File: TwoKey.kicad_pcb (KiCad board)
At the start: 2 copper layers, 34 parts, among them J1 USB_C_Receptacle_USB2.0, SW1 SW_SPST, SW2 SW_SPST, SW3 BOOTSEL, SW4 RESET, U1 AMS1117-3.3, U2 W25Q128JVS, U3 RP2040TR7, X1 OSC

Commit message: Started work on condencing items
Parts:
- J1: moved to B.Cu
- moved C1 50.5 mm to (33.3, 43.0)
- moved C2 50.5 mm to (41.0, 37.7)
- moved U1 50.5 mm to (35.7, 38.5)
- moved C10 50.1 mm to (70.7, 58.4)
- moved C11 50.1 mm to (64.8, 63.5)
- moved C12 50.1 mm to (58.3, 64.8)
- moved C13 50.1 mm to (58.5, 58.4)
- moved C14 50.1 mm to (58.5, 54.8)
- moved C16 50.1 mm to (69.8, 51.3)
- moved C6 50.1 mm to (66.8, 51.3)
- moved C8 50.1 mm to (68.3, 51.3)
- moved C9 50.1 mm to (70.7, 54.8)
- moved R7 50.1 mm to (63.3, 65.4)
- moved U2 50.1 mm to (56.8, 49.8)
- moved U3 50.1 mm to (64.6, 57.4)
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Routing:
- net +5V: track 2.21 -> 9.57 mm
- net /USB_DN: track 0.00 -> 2.99 mm, vias 0 -> 1
- net /USB_DP: track 0.00 -> 2.91 mm, vias 0 -> 1
- net GND: track 0.00 -> 2.31 mm, vias 0 -> 2
- net Net-(R6-Pad1): track 4.50 -> 5.70 mm
- net Net-(R5-Pad1): track 4.50 -> 5.70 mm

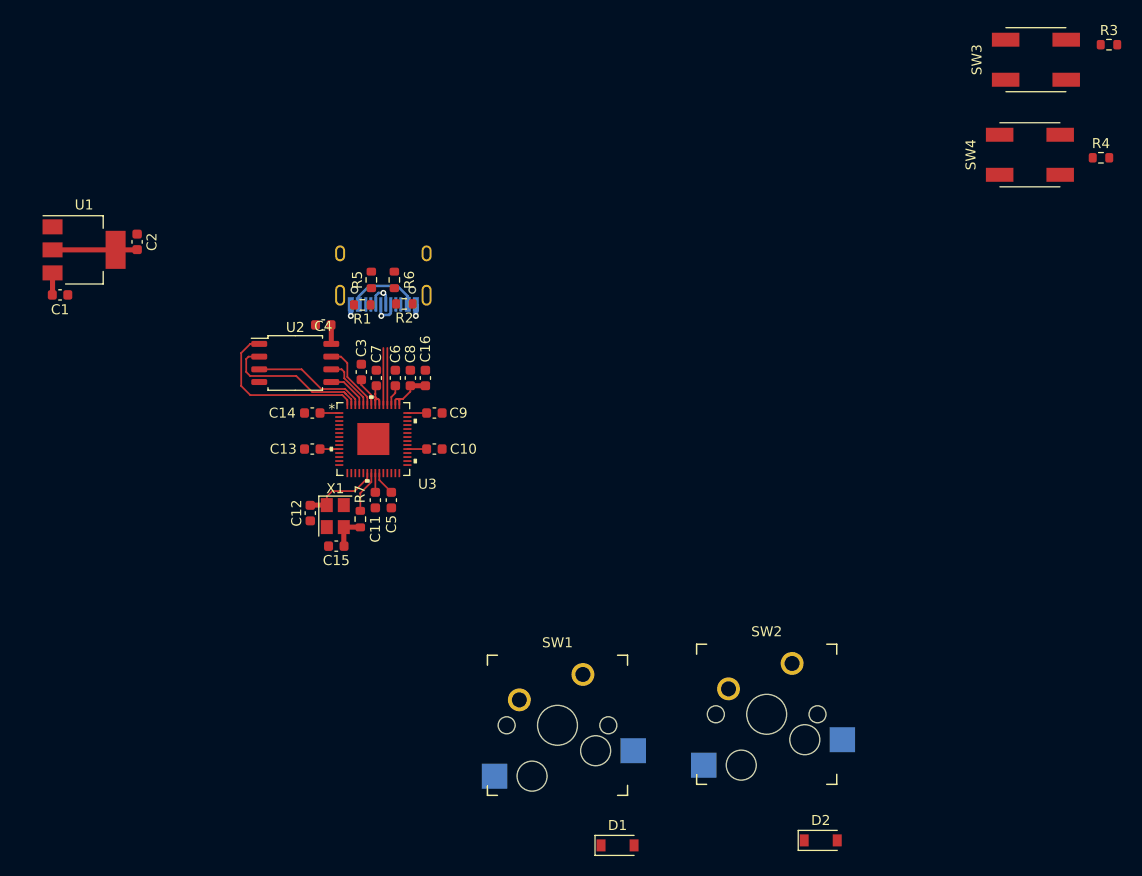
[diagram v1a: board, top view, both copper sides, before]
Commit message: Reworked some placement and added submodule
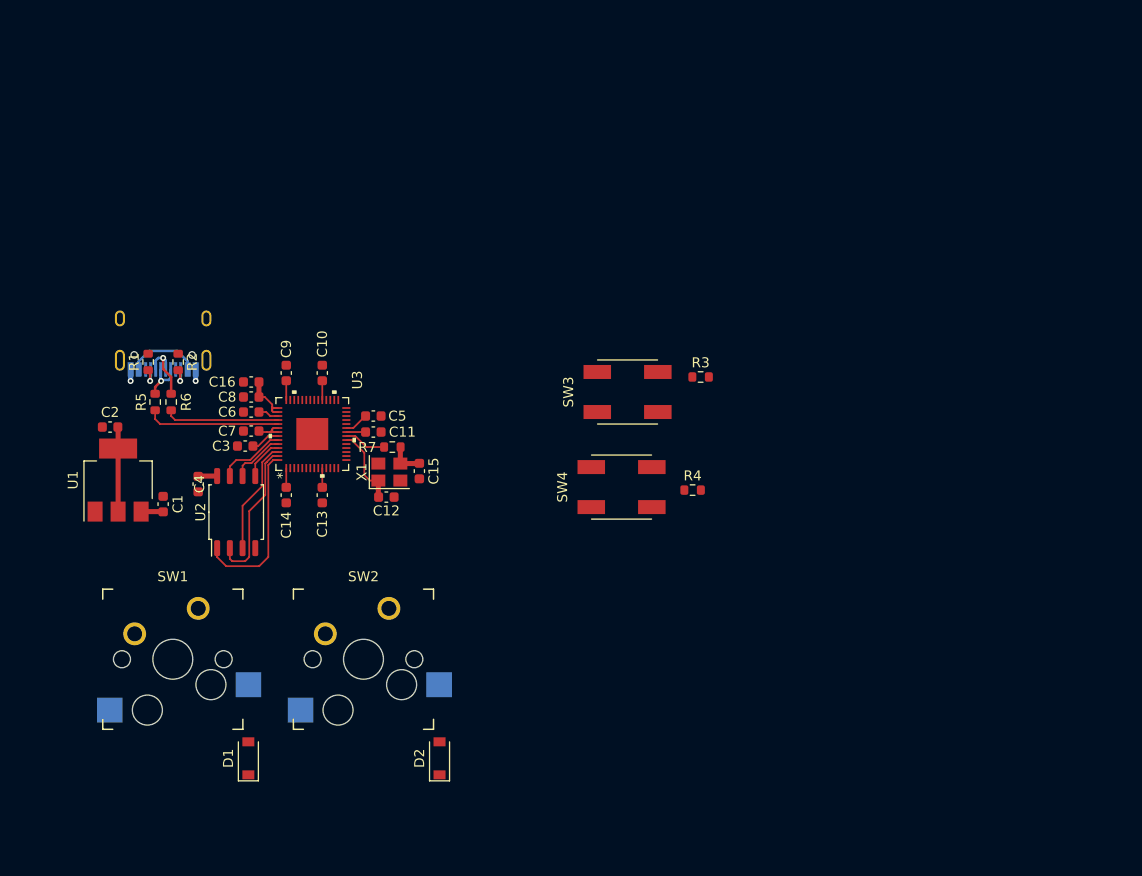
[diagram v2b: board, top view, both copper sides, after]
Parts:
- moved R4 52.6 mm to (96.5, 62.5)
- moved SW3 52.6 mm to (90.0, 52.7)
- moved R3 52.6 mm to (97.3, 51.2)
- moved SW4 52.6 mm to (89.4, 62.2)
- moved SW2 40.7 mm to (63.6, 79.4)
- moved SW1 39.0 mm to (44.6, 79.4)
- moved D2 39.0 mm to (71.2, 89.3), turned to 90 degrees
- moved D1 37.9 mm to (52.1, 89.3), turned to 90 degrees
- moved R6 25.4 mm to (44.4, 53.7), turned to 90 degrees
- moved R5 24.8 mm to (42.8, 53.7), turned to 90 degrees
- moved R2 23.3 mm to (45.1, 49.7), turned to 90 degrees
- moved C1 23.3 mm to (43.6, 63.9), turned to 90 degrees
- moved U1 23.2 mm to (39.1, 61.5), turned to 90 degrees
- moved J1 22.9 mm to (43.6, 46.4)
- moved R1 22.1 mm to (42.1, 49.7), turned to 90 degrees
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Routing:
- net Net-(R5-Pad1): track 5.70 -> 13.4 mm
- net Net-(R6-Pad1): track 5.70 -> 11.4 mm
- net /USB_DN: track 2.99 -> 6.90 mm
- net Net-(J1-PadB5): track 0.00 -> 2.33 mm, vias 0 -> 1
- net Net-(J1-PadA5): track 0.00 -> 2.33 mm, vias 0 -> 1
- net /USB_DP: track 2.91 -> 4.43 mm

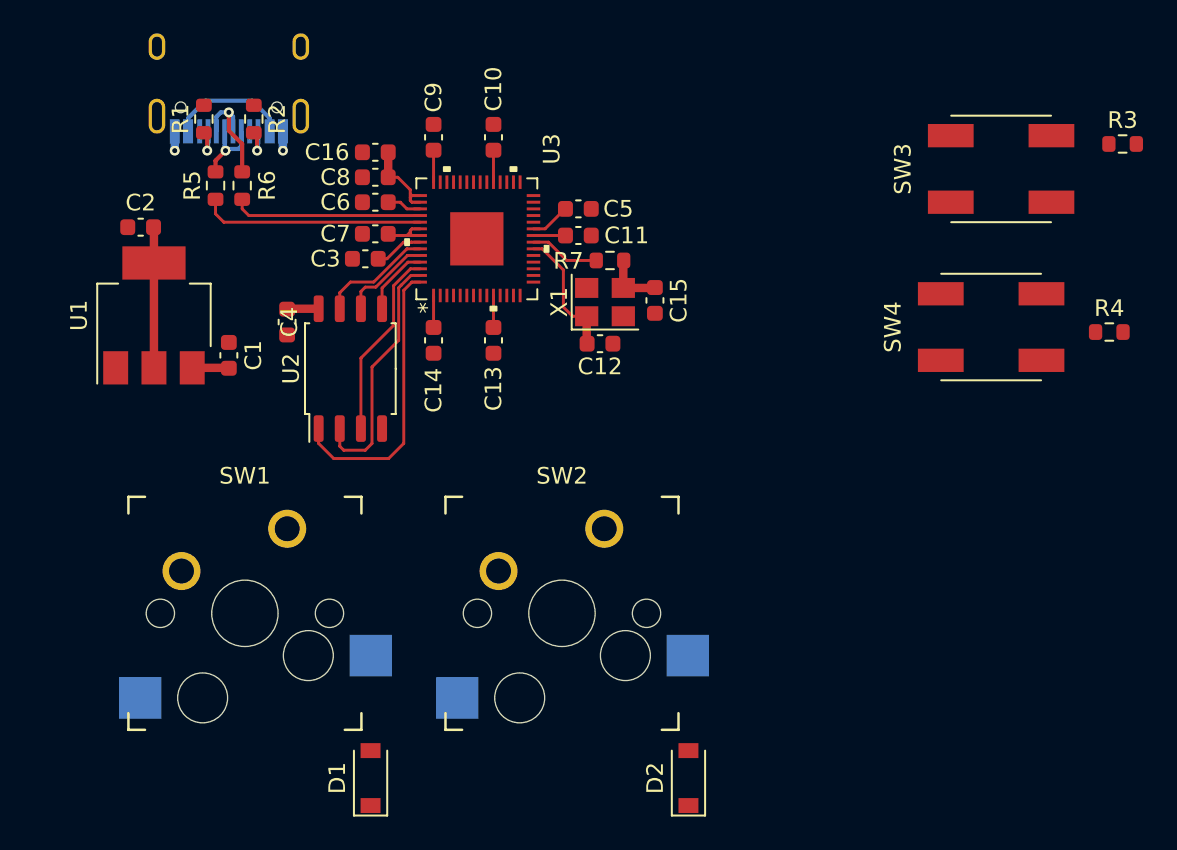
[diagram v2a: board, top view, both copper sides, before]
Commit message: Condenced items into initial pcb
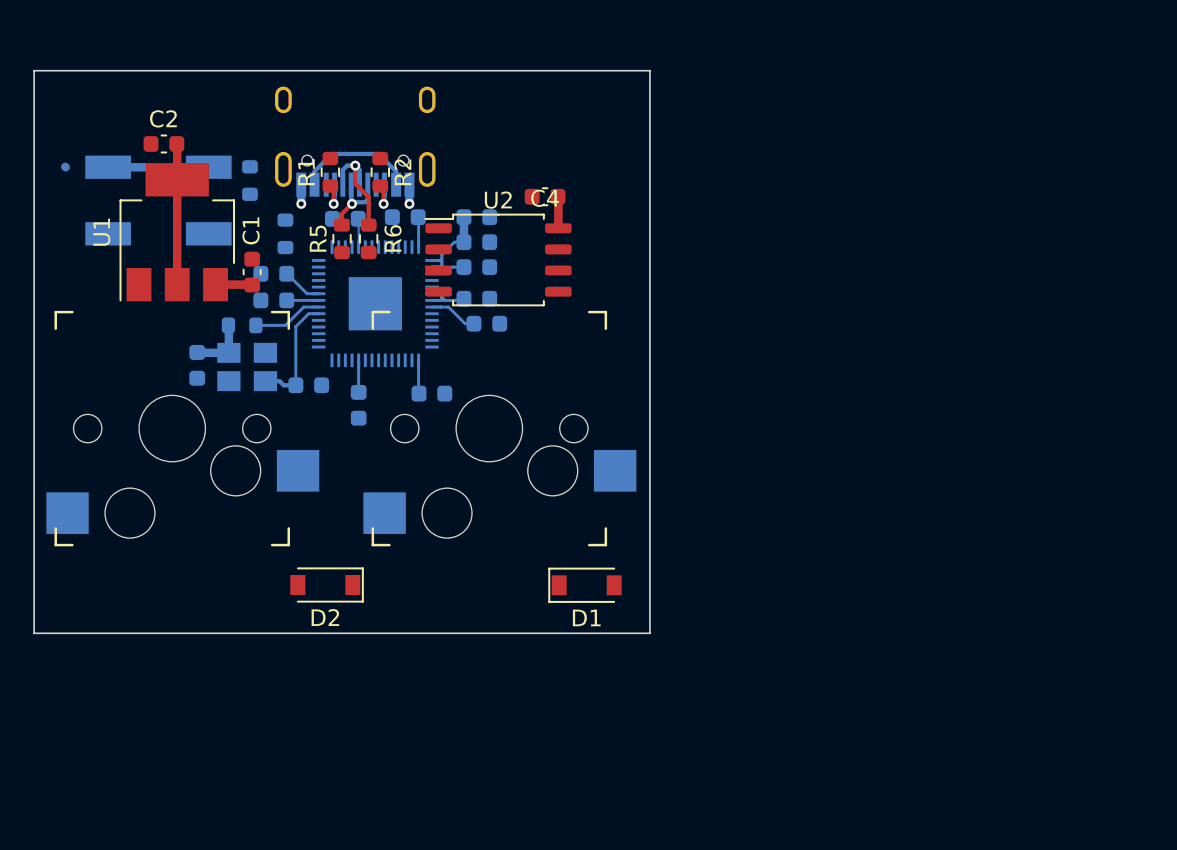
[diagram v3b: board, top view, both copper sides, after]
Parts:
- removed SW4: RESET, TwoKey:DTSL-61N-V
- C10, C11, C12, C13, C14, C15, C16, C3, C5, C6, C7, C8, C9, R3, R4, R7, SW3, U3, X1: moved to B.Cu
- SW1, SW2: footprint keyswitches:Kailh_socket_MX_optional -> keyswitches:Kailh_socket_MX
- moved R3 52.5 mm to (44.9, 53.4), turned to 90 degrees
- moved SW3 50.7 mm to (39.4, 54.6), turned to 180 degrees
- moved R4 49.9 mm to (47.0, 56.6), turned to -90 degrees
- moved C15 27.8 mm to (41.7, 64.5)
- moved SW2 25.9 mm to (40.2, 68.3), turned to 180 degrees
- moved D2 24.7 mm to (49.4, 77.7), turned to 180 degrees
- moved R7 22.4 mm to (44.4, 62.1), turned to 0 degrees
- moved X1 21.9 mm to (44.7, 64.6), turned to 180 degrees
- moved C11 18.7 mm to (46.3, 60.6), turned to 180 degrees
- moved C5 18.7 mm to (46.3, 59.0), turned to 180 degrees
- moved SW1 18.4 mm to (59.2, 68.3), turned to 180 degrees
- moved C12 17.7 mm to (48.4, 65.7)
- moved D1 17.4 mm to (65.1, 77.7), turned to 0 degrees
- moved C4 17.2 mm to (62.6, 54.4), turned to 180 degrees
- moved U2 11.0 mm to (59.8, 58.2), turned to 0 degrees
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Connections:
- SW1 pad 1: /COL1 -> Net-(D1-Pad2)
- SW1 pad 2: Net-(D1-Pad2) -> /COL1
- SW2 pad 1: /COL2 -> Net-(D2-Pad2)
- SW2 pad 2: Net-(D2-Pad2) -> /COL2
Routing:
- net /QSPI_SS: track 17.2 -> 0.00 mm
- net /QSPI_SD1: track 15.0 -> 0.00 mm
- net Net-(R5-Pad1): track 13.4 -> 0.00 mm
- net Net-(R6-Pad1): track 11.4 -> 0.00 mm
- net /QSPI_SD2: track 11.4 -> 0.00 mm
- net /QSPI_SD3: track 6.89 -> 0.00 mm
- net Net-(R3-Pad2): track 0.00 -> 6.09 mm
- net /QSPI_SCLK: track 5.49 -> 0.00 mm
- net /QSPI_SD0: track 4.18 -> 0.00 mm
- net /XIN: track 7.84 -> 7.15 mm
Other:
- board outline added: 37 x 33.8 mm

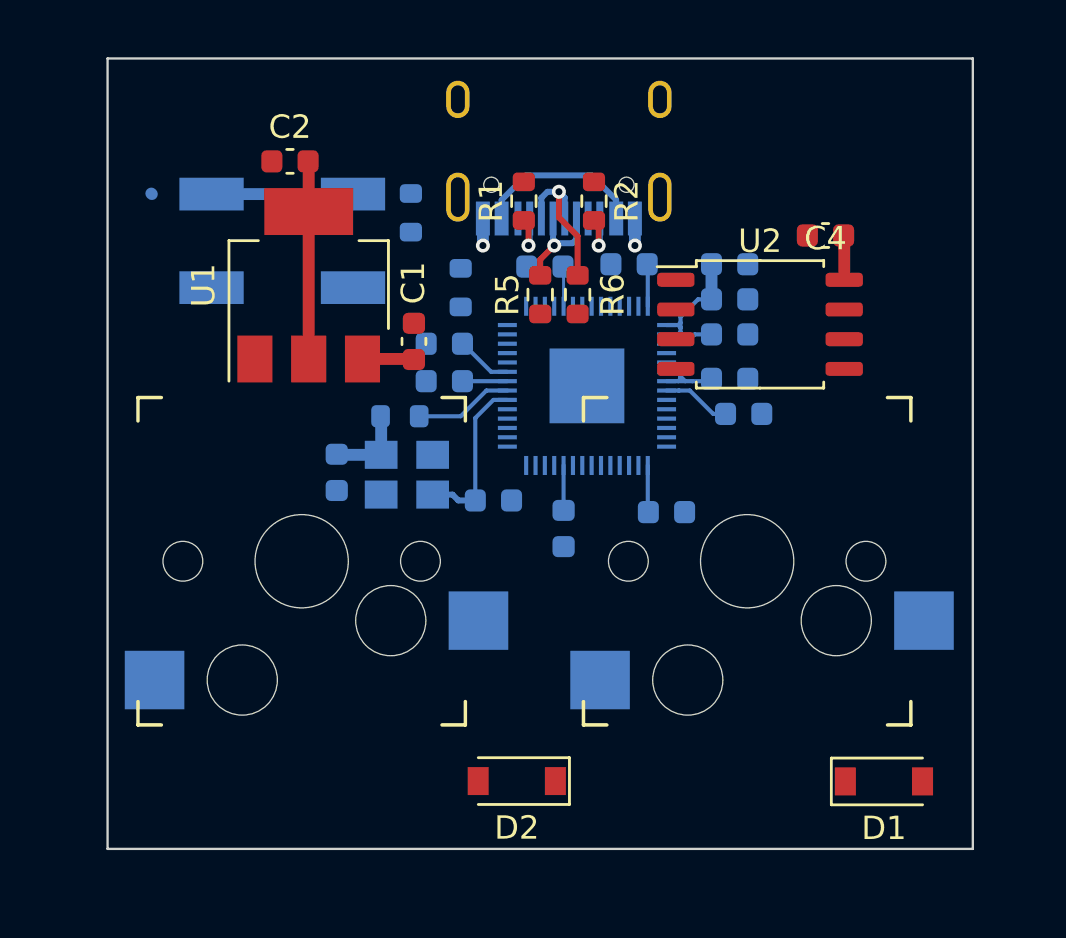
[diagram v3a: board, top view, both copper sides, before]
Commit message: Readjusted more componenets (DRC not passing)
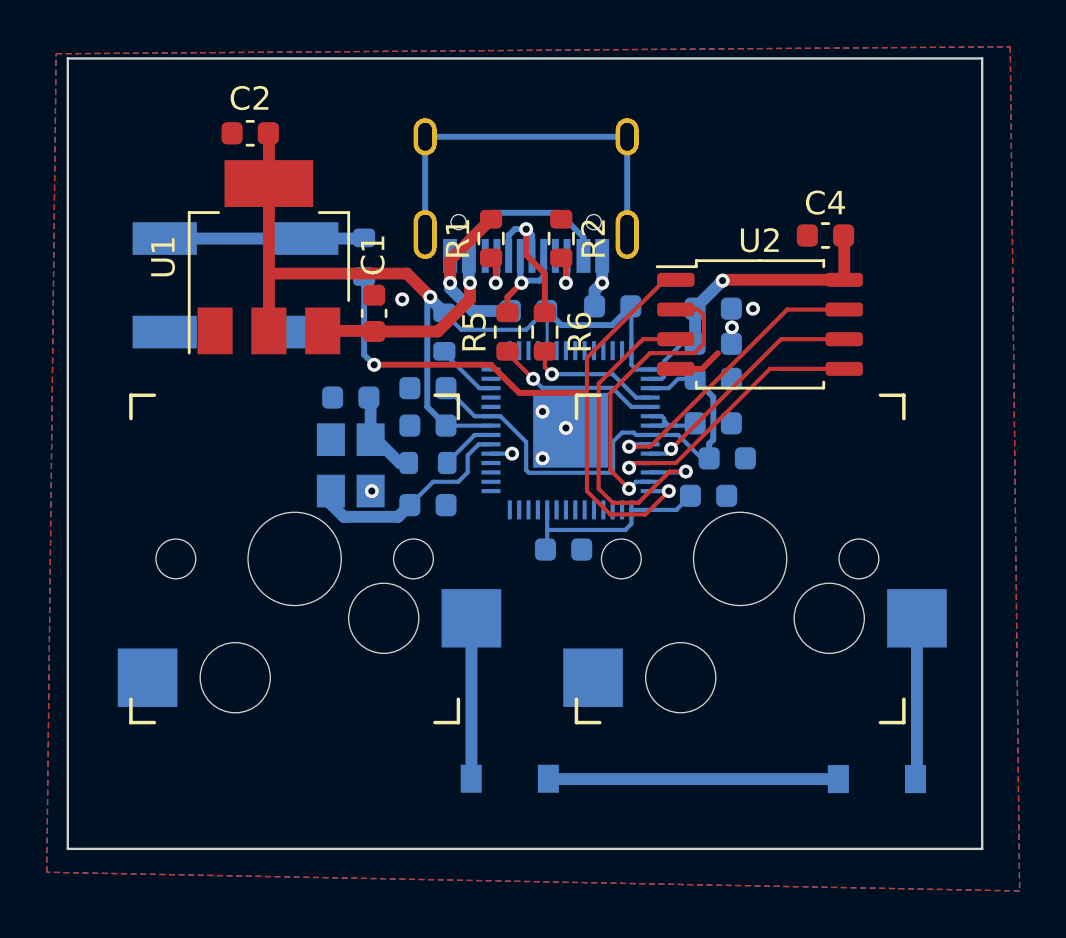
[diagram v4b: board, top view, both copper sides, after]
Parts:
- D1, D2: moved to B.Cu
- moved C15 3.26 mm to (42.3, 61.3), turned to 180 degrees
- moved C12 2.81 mm to (45.6, 65.9)
- moved R3 2.76 mm to (42.9, 55.3)
- moved SW3 2.76 mm to (37.4, 56.5)
- moved X1 2.43 mm to (42.3, 64.2), turned to 90 degrees
- moved R7 2.33 mm to (45.6, 64.1)
- moved J1 2.13 mm to (49.8, 51.2)
- moved R1 2.13 mm to (48.3, 54.5)
- moved R2 2.13 mm to (51.3, 54.5)
- moved R5 2.13 mm to (49.0, 58.5)
- moved R6 2.13 mm to (50.6, 58.5)
- moved C2 2.08 mm to (38.0, 50.0)
- moved U1 2.08 mm to (38.8, 55.3)
- moved C1 2.08 mm to (43.3, 57.7)
- moved U3 2.02 mm to (51.7, 62.7)
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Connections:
- SW1 pad 1: Net-(D1-Pad2) -> /COL1
- SW1 pad 2: /COL1 -> Net-(D1-Pad2)
- SW2 pad 1: Net-(D2-Pad2) -> /COL2
- SW2 pad 2: /COL2 -> Net-(D2-Pad2)
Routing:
- net +3V3: track 28.6 -> 65.4 mm, vias 0 -> 2
- net /QSPI_SS: track 0.00 -> 29.5 mm, vias 0 -> 2
- net unconnected-(J1-PadS1): track 0.00 -> 17.0 mm
- net /QSPI_SD2: track 0.00 -> 14.7 mm, vias 0 -> 1
- net +1V1: track 7.44 -> 21.3 mm
- net /QSPI_SD1: track 0.00 -> 12.8 mm, vias 0 -> 1
- net /QSPI_SD3: track 0.00 -> 12.6 mm, vias 0 -> 1
- net /ROW1: track 0.00 -> 12.4 mm
- net /QSPI_SD0: track 0.00 -> 11.9 mm, vias 0 -> 1
- net GND: track 2.31 -> 13.1 mm, vias 2 -> 10
- net /QSPI_SCLK: track 0.00 -> 10.3 mm, vias 0 -> 1
- net Net-(R5-Pad1): track 0.00 -> 7.13 mm, vias 0 -> 1
- net Net-(D1-Pad2): track 0.00 -> 6.90 mm
- net Net-(D2-Pad2): track 0.00 -> 6.86 mm
- net +5V: track 9.57 -> 16.1 mm, vias 0 -> 1
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- added copper zone on B.Cu, net GND
- added copper zone on F.Cu, net GND
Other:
- board size 37 x 33.8 mm -> 39.1 x 33.8 mm

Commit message: Finished routing of all traces
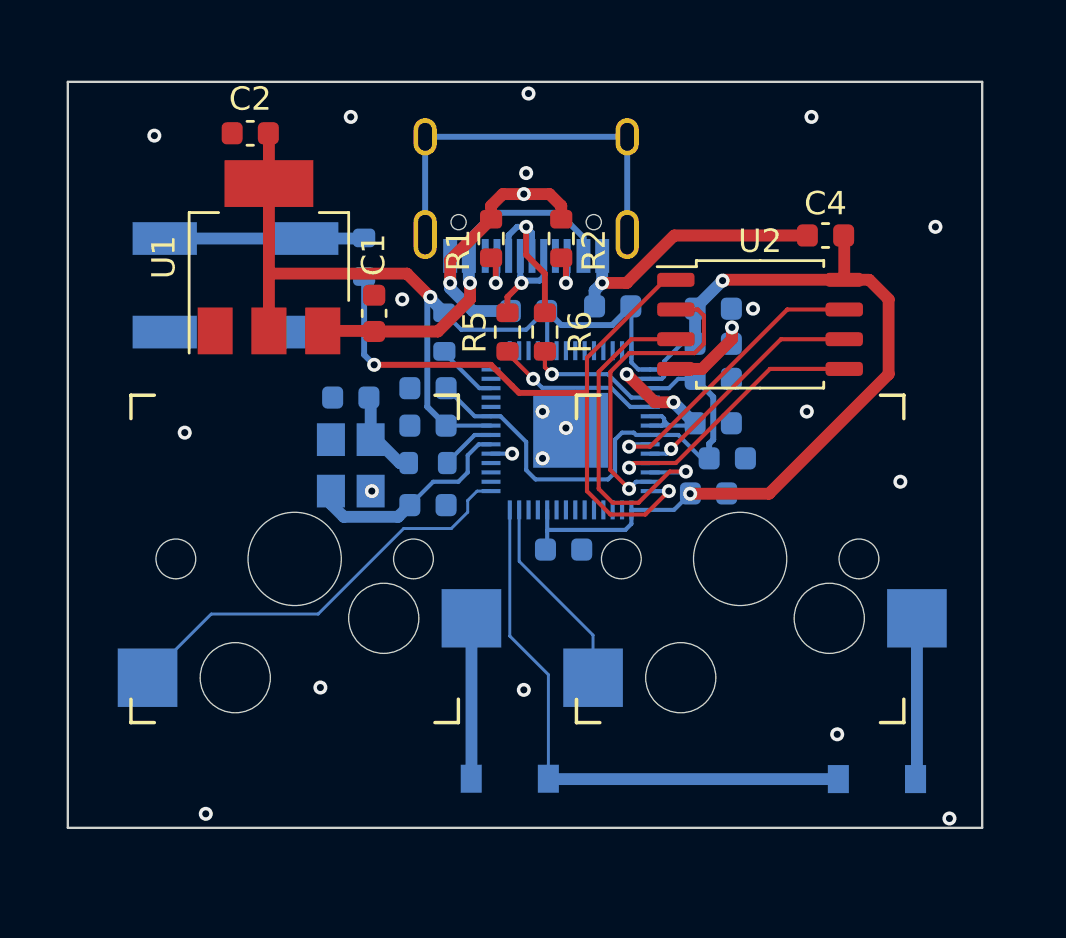
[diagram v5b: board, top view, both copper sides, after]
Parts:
- moved C14 0.10 mm to (57.6, 65.4)
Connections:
- U3 pad 13: unconnected-(U3-Pad13) -> /COL1
- U3 pad 14: unconnected-(U3-Pad14) -> /ROW1
- U3 pad 15: unconnected-(U3-Pad15) -> /COL2
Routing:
- net +3V3: track 65.4 -> 85.8 mm, vias 2 -> 5
- net /COL2: track 0.00 -> 18.3 mm
- net GND: track 13.1 -> 28.6 mm, vias 10 -> 25
- net /ROW1: track 12.4 -> 24.6 mm
- net /COL1: track 0.00 -> 8.49 mm
- net /QSPI_SD1: track 12.8 -> 13.4 mm
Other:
- board size 39.1 x 33.8 mm -> 39.1 x 31.9 mm
